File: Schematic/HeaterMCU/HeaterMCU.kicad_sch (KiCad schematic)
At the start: 48 parts, among them J1 MCU_Interface, J2 Firmware, SW1 RESET, U1 AMS1117-3.3, U2 Display_IPS_1.3_SPI, U3 ATMEGA328P-AU, U4 INA219AIDCNR, U5 TPS54302, Y1 16MHz

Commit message: First draft
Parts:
- C1, C10, C11, C12, C13, C14, C15, C16, C3, C4, C5, C6, C7, C8, C9: footprint Capacitor_SMD:C_0805_2012Metric_Pad1.18x1.45mm_HandSolder -> Capacitor_SMD:C_0603_1608Metric_Pad1.08x0.95mm_HandSolder
- R1, R11, R12, R13, R14, R2, R3, R4, R5, R6, R7, R8: footprint Resistor_SMD:R_0805_2012Metric_Pad1.20x1.40mm_HandSolder -> Resistor_SMD:R_0603_1608Metric_Pad0.98x0.95mm_HandSolder
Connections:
- net FlagHighVoltage: now also R2.2, U3.19 (A6); no longer R1.2, U3.1 (D3(PWM)/INT1)
- net FlagMBHeaterActive: now also R1.2, U3.22 (A7); no longer R2.2, U3.2 (D4)
- net GNDPWR: now also D1.1 (K), D2.1 (K), D3.1 (K); no longer R3.1, R4.1, R5.1
- net Heater_EN: now also U3.23 (A0); no longer U3.24 (A1)
- net LED_Heater_ON: now also R4.2, U3.9 (D5(PWM)); no longer D2.2 (A), U3.26 (A3)
- net LED_Heater_Start: now also R5.2, U3.10 (D6(PWM)); no longer D3.2 (A), U3.9 (D5(PWM))
- net LED_MCU_ON: now also R3.2, U3.14 (D10(PWM)/SS); no longer D1.2 (A), U3.32 (D2/INT0)
- net RLY_CTRL: now also U3.24 (A1); no longer U3.23 (A0)
- new net: D2.2 (A), R4.1
- new net: D3.2 (A), R5.1
- new net: D1.2 (A), R3.1
- no-connect marks 9 -> 7
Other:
- moved on the sheet: C8, D1, D2, D3, R1, R2, R3, R4, R5

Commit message: Minor layout changes
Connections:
- no-connect marks 7 -> 10
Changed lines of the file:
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@@
   )
   (no_connect (at 133.985 78.105))
+  (no_connect (at 133.985 106.045))
+  (no_connect (at 133.985 121.285))
   (no_connect (at 95.885 133.35))
   (no_connect (at 64.77 165.735))
   (no_connect (at 133.985 85.725))
+  (no_connect (at 133.985 103.505))
   (no_connect (at 133.985 57.785))
   (no_connect (at 133.985 60.325))
@@
     (stroke (width 0) (type default) (color 0 0 0 0))
   )
-  (wire (pts (xy 131.445 103.505) (xy 133.985 103.505))
-    (stroke (width 0) (type default) (color 0 0 0 0))
-  )
   (wire (pts (xy 250.825 53.34) (xy 251.46 53.34))
     (stroke (width 0) (type default) (color 0 0 0 0))
@@
     (stroke (width 0) (type default) (color 0 0 0 0))
   )
-  (wire (pts (xy 131.445 106.045) (xy 133.985 106.045))
-    (stroke (width 0) (type default) (color 0 0 0 0))
-  )
   (wire (pts (xy 93.345 131.445) (xy 93.345 133.35))
     (stroke (width 0) (type default) (color 0 0 0 0))
@@
     (stroke (width 0) (type default) (color 0 0 0 0))
   )
-  (wire (pts (xy 131.445 121.285) (xy 133.985 121.285))
-    (stroke (width 0) (type default) (color 0 0 0 0))
-  )

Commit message: Updated annotation
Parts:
- renumbered C1 to C301, C3 to C302, C4 to C303, C5 to C304, C6 to C305, C7 to C306, C8 to C307, C9 to C308, C10 to C309, C11 to C310, C12 to C311, C13 to C312, C14 to C313, C15 to C314, C16 to C315, D1 to D301, D2 to D302, D3 to D303, D4 to D304, FB1 to FB301, H1 to H301, H2 to H302, H3 to H303, H4 to H304, J1 to J301, J2 to J302, L1 to L301, R1 to R301, R2 to R302, R3 to R303, R4 to R304, R5 to R305, R6 to R306, R7 to R307, R8 to R308, R9 to R309, R10 to R310, R11 to R311, R12 to R312, R13 to R313, R14 to R314, SW1 to SW301, U1 to U301, U2 to U302, U3 to U303, U4 to U304, U5 to U305, Y1 to Y301

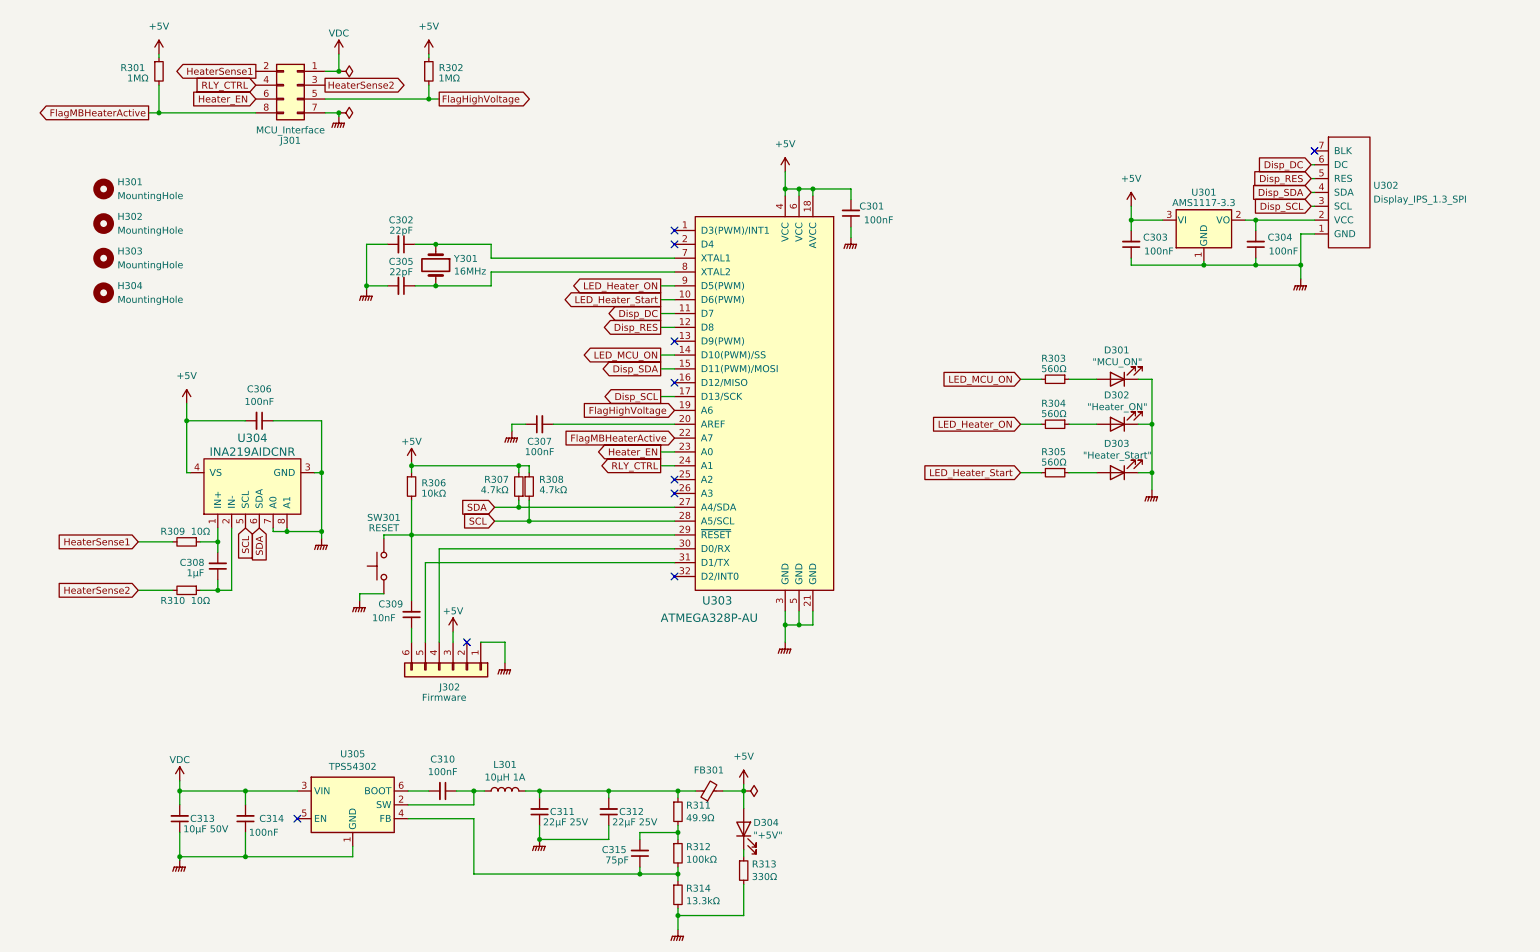
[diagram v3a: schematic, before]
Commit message: MCU Board adapted for 3.3V operation
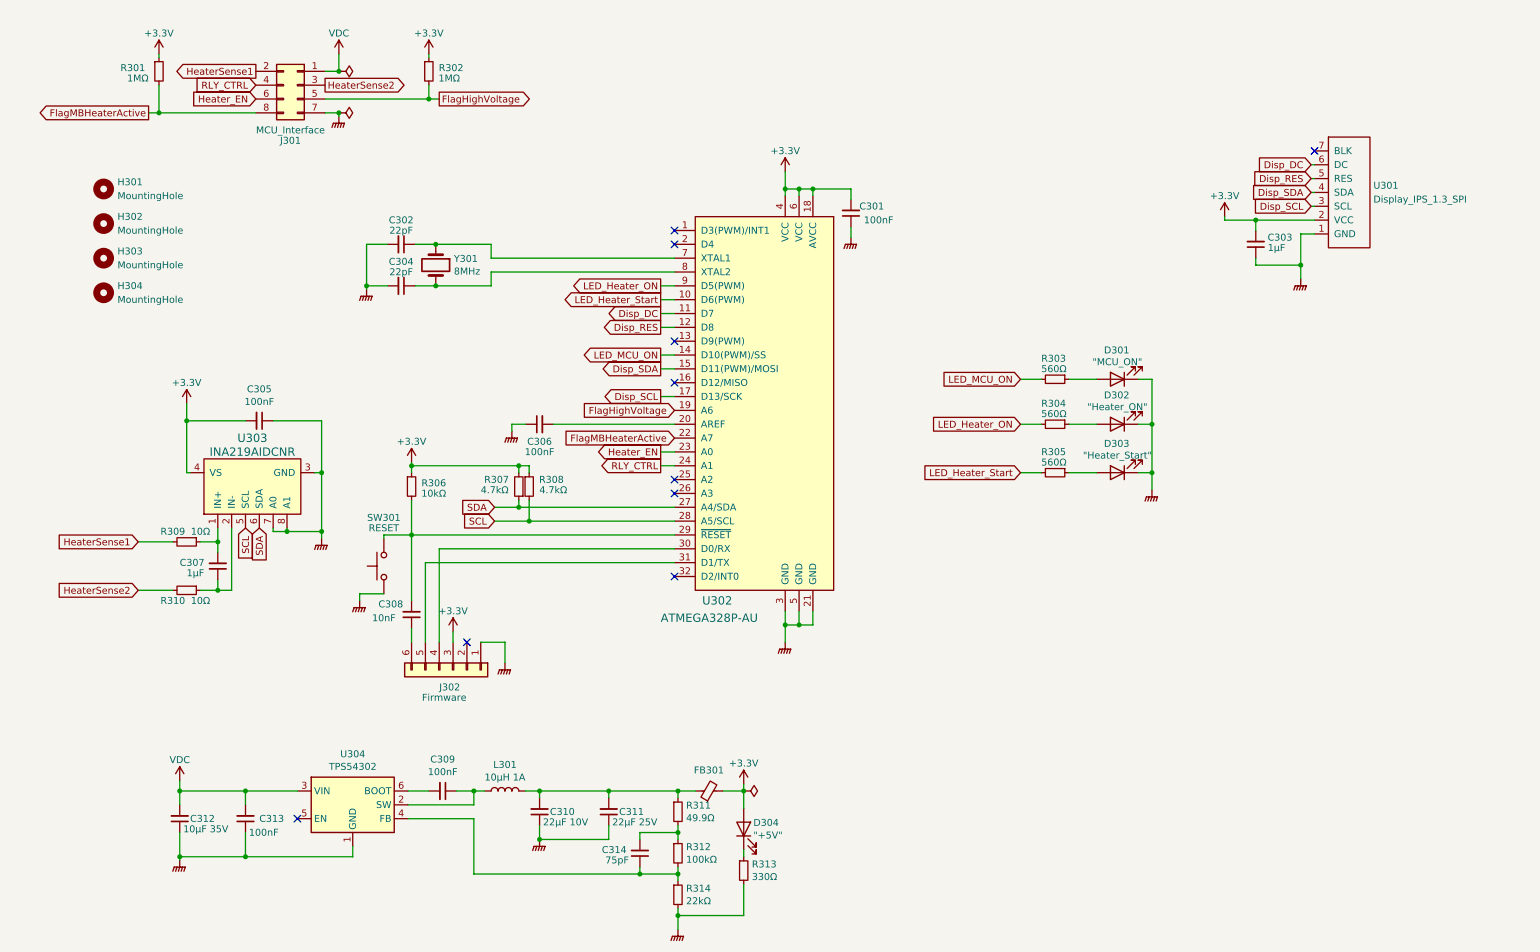
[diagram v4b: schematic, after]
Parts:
- removed C303: 100nF, Capacitor_SMD:C_0603_1608Metric_Pad1.08x0.95mm_HandSolder, symbol Device:C_Small
- removed U301: AMS1117-3.3, Package_TO_SOT_SMD:SOT-223-3_TabPin2, symbol Regulator_Linear:AMS1117-3.3
- C303: renamed from C304; value 100nF -> 1µF
- C310: renamed from C311; value 22µF 25V -> 22µF 10V
- C312: renamed from C313; value 10µF 50V -> 10µF 35V
- R309, R310: footprint Resistor_SMD:R_0805_2012Metric_Pad1.20x1.40mm_HandSolder -> Resistor_SMD:R_0603_1608Metric_Pad0.98x0.95mm_HandSolder
- R314: value 13.3kΩ -> 22kΩ
- Y301: value 16MHz -> 8MHz
- renumbered C305 to C304, C306 to C305, C307 to C306, C308 to C307, C309 to C308, C310 to C309, C312 to C311, C314 to C313, C315 to C314, U302 to U301, U303 to U302, U304 to U303, U305 to U304
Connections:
- net +5V is gone; now on net +3V3: C301.2, C305.2, D304.2 (A), FB301.2, J302.3 (Pin_3), R301.1, R302.1, R306.1, R307.2, R308.1, U302.18 (AVCC), U302.4 (VCC), U302.6 (VCC), U303.4 (VS)
- net +3V3: now reaches C303.2, U301.2 (VCC)

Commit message: Optocouplers moved to from PSU to MCU board
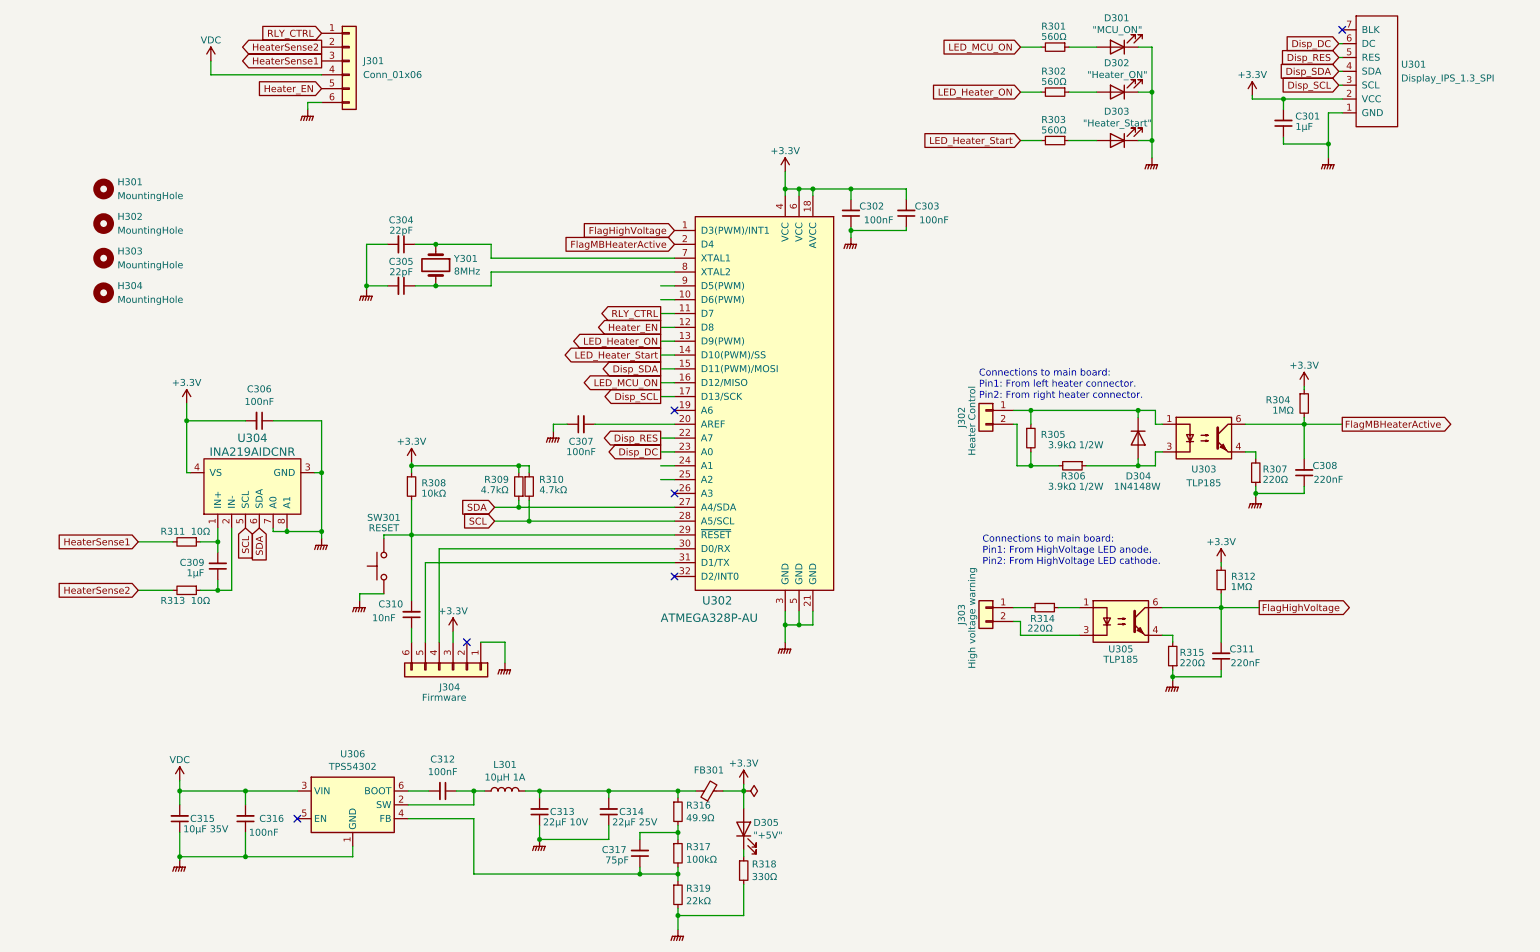
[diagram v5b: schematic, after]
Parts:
- removed J301: MCU_Interface, Connector_PinHeader_2.54mm:PinHeader_2x04_P2.54mm_Vertical, symbol Connector_Generic:Conn_02x04_Odd_Even
- added C303: 100nF, Capacitor_SMD:C_0603_1608Metric_Pad1.08x0.95mm_HandSolder, symbol Device:C_Small
- added C308, C311: 220nF, Capacitor_SMD:C_0603_1608Metric_Pad1.08x0.95mm_HandSolder, symbol Device:C_Small
- added D304: 1N4148W, Diode_SMD:D_SOD-123, symbol Diode:1N4148W
- added J301: Conn_01x06, Connector_PinSocket_2.54mm:PinSocket_1x06_P2.54mm_Vertical, symbol Connector_Generic:Conn_01x06
- added J302: Heater Control, Connector_PinSocket_2.54mm:PinSocket_1x02_P2.54mm_Horizontal, symbol Connector_Generic:Conn_01x02
- added J303: High voltage warning, Connector_PinSocket_2.54mm:PinSocket_1x02_P2.54mm_Horizontal, symbol Connector_Generic:Conn_01x02
- added R305, R306: 3.9kΩ 1/2W, Resistor_SMD:R_1210_3225Metric_Pad1.30x2.65mm_HandSolder, symbol Device:R_Small
- added R307, R314, R315: 220Ω, Resistor_SMD:R_0603_1608Metric_Pad0.98x0.95mm_HandSolder, symbol Device:R_Small
- added U303, U305: TLP185, Package_SO:SOIC-4_4.55x3.7mm_P2.54mm, symbol Isolator:TLP185
- D301, D302, D303: footprint LED_SMD:LED_0805_2012Metric_Pad1.15x1.40mm_HandSolder -> LED_SMD:LED_0603_1608Metric_Pad1.05x0.95mm_HandSolder
- D305: renamed from D304; footprint LED_SMD:LED_0805_2012Metric_Pad1.15x1.40mm_HandSolder -> LED_SMD:LED_0603_1608Metric_Pad1.05x0.95mm_HandSolder
- FB301: footprint Inductor_SMD:L_0805_2012Metric_Pad1.15x1.40mm_HandSolder -> Inductor_SMD:L_0603_1608Metric_Pad1.05x0.95mm_HandSolder
- SW301: footprint Button_Switch_SMD:SW_SPST_CK_RS282G05A3 -> myDevices:Tactile_sw_SMD_side_01
- renumbered C303 to C301, C301 to C302, C302 to C304, C304 to C305, C305 to C306, C306 to C307, C307 to C309, C308 to C310, C309 to C312, C310 to C313, C311 to C314, C312 to C315, C313 to C316, C314 to C317, J302 to J304, R303 to R301, R304 to R302, R305 to R303, R301 to R304, R306 to R308, R307 to R309, R308 to R310, R309 to R311, R302 to R312, R310 to R313, R311 to R316, R312 to R317, R313 to R318, R314 to R319, U303 to U304, U304 to U306
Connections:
- net +3V3: now also C303.2
- net Disp_DC: now also U302.23 (A0); no longer U302.11 (D7)
- net Disp_RES: now also U302.22 (A7); no longer U302.12 (D8)
- net FlagHighVoltage: now also U302.1 (D3(PWM)/INT1), C311.2, U305.6; no longer U302.19 (A6)
- net FlagMBHeaterActive: now also U302.2 (D4), C308.2, U303.6; no longer U302.22 (A7)
- net GNDPWR: now also C303.1, C308.1, C311.1, J301.6 (Pin_6), R307.1, R315.1
- net HeaterSense1: now also J301.3 (Pin_3)
- net HeaterSense2: now also J301.2 (Pin_2)
- net Heater_EN: now also U302.12 (D8), J301.5 (Pin_5); no longer U302.23 (A0)
- net LED_Heater_ON: now also U302.13 (D9(PWM)); no longer U302.9 (D5(PWM))
- net LED_Heater_Start: now also U302.14 (D10(PWM)/SS); no longer U302.10 (D6(PWM))
- net LED_MCU_ON: now also U302.16 (D12/MISO); no longer U302.14 (D10(PWM)/SS)
- net RLY_CTRL: now also U302.11 (D7), J301.1 (Pin_1); no longer U302.24 (A1)
- net VDC: now also J301.4 (Pin_4)
- new net: D304.1 (K), J302.1 (Pin_1), R305.1, U303.1
- new net: J302.2 (Pin_2), R305.2, R306.2
- new net: R314.1, U305.1
- new net: J303.2 (Pin_2), U305.3
- new net: R315.2, U305.4
- new net: J303.1 (Pin_1), R314.2
- new net: R307.2, U303.4
- new net: D304.2 (A), R306.1, U303.3
- no-connect marks 10 -> 6
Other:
- note added: "Connections to main board: Pin1: From HighVoltage LED anode. Pin2: From HighVoltage LED cathode."
- note added: "Connections to main board: Pin1: From left heater connector. Pin2: From right heater connector."
- moved on the sheet: C301, C307, D301, D302, D303, R301, R302, R303, R304, R312, U301

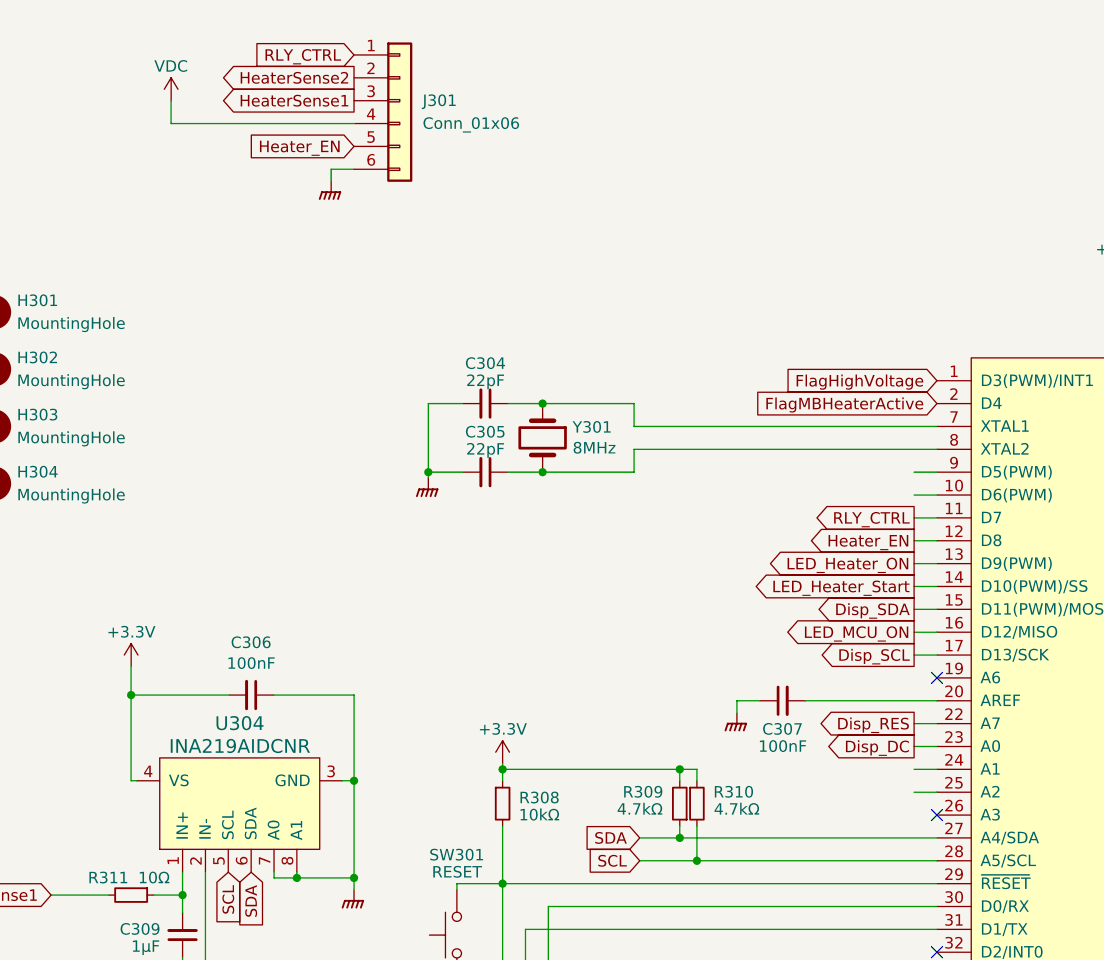
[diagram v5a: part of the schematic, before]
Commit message: Swapped IO pins
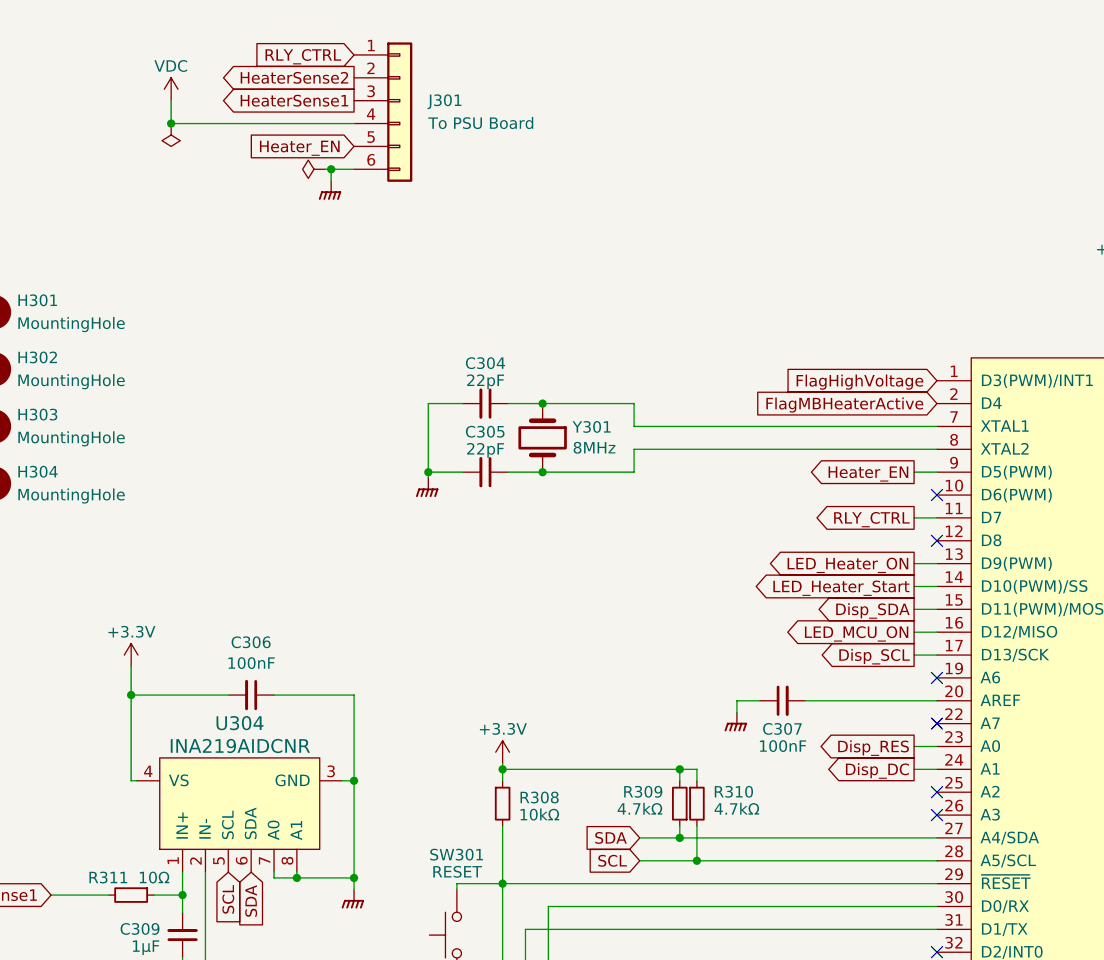
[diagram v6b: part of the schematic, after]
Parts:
- J301: value Conn_01x06 -> To PSU Board
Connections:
- net Disp_DC: now also U302.24 (A1); no longer U302.23 (A0)
- net Disp_RES: now also U302.23 (A0); no longer U302.22 (A7)
- net Heater_EN: now also U302.9 (D5(PWM)); no longer U302.12 (D8)
- no-connect marks 6 -> 10
